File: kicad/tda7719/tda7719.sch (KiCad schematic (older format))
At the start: 15 parts

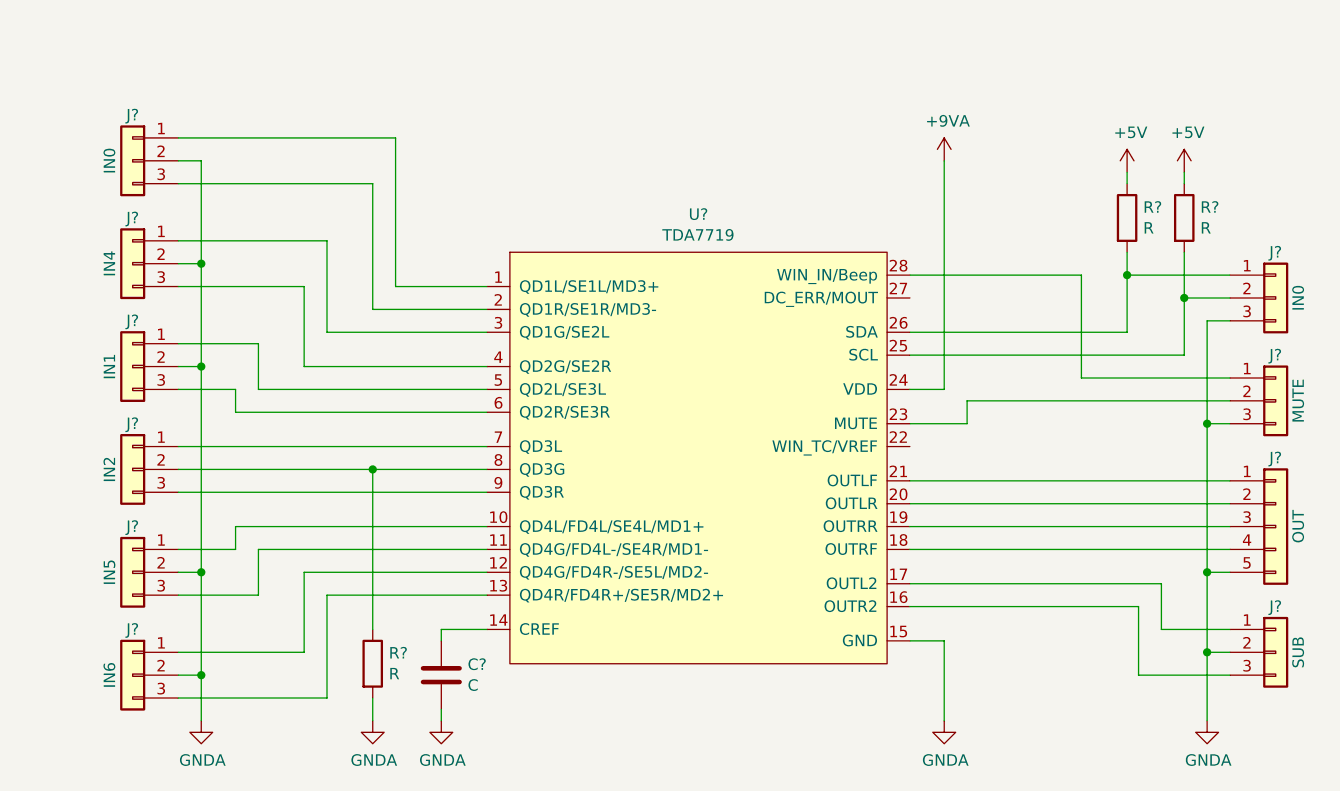
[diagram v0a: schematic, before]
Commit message: PCB for TDA7719
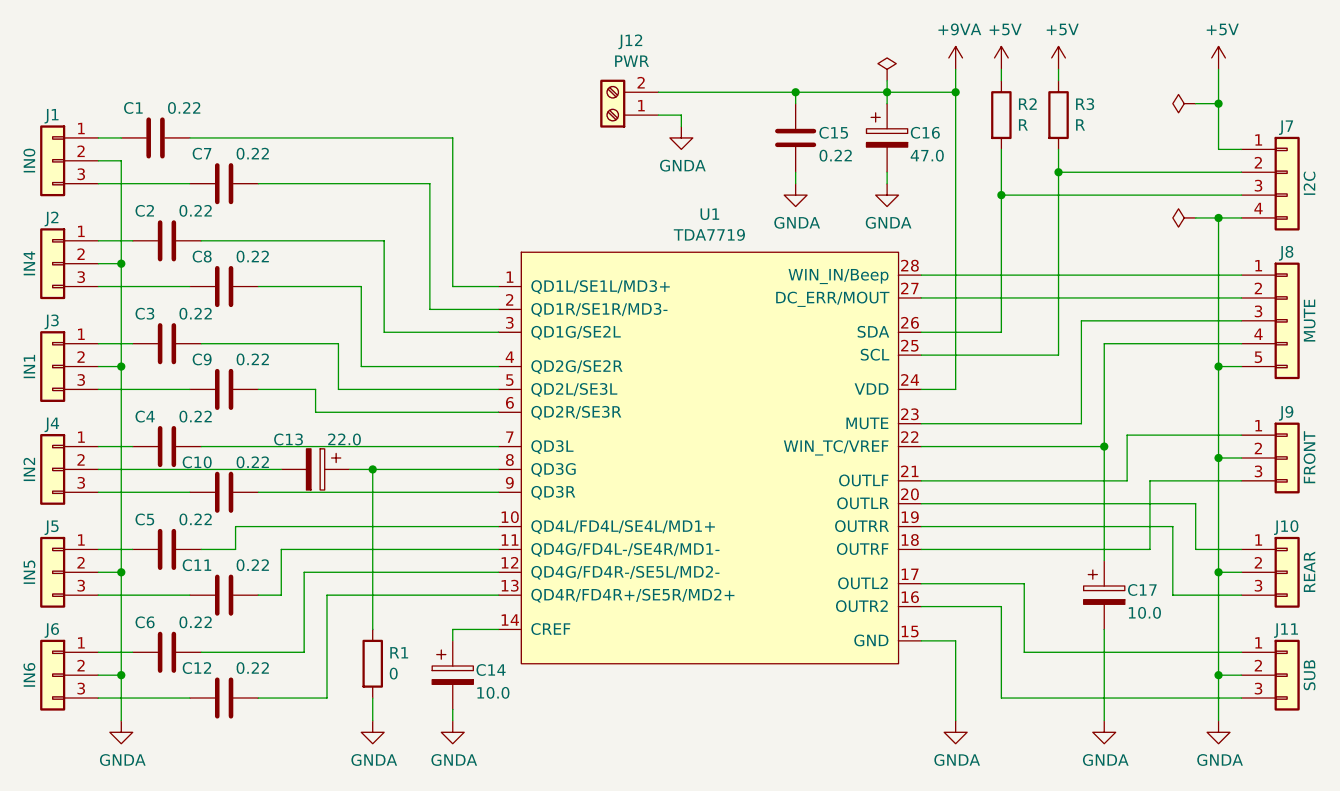
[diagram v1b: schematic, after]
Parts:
- removed C?: C, symbol Device:C
- removed J?: OUT, symbol Connector_Generic:Conn_01x05
- removed J?: IN0, symbol Connector_Generic:Conn_01x03
- removed J?: MUTE, symbol Connector_Generic:Conn_01x03
- added C1, C10, C11, C12, C15, C2, C3, C4, C5, C6, C7, C8, C9: 0.22, Capacitor_SMD:C_1206_3216Metric_Pad1.42x1.75mm_HandSolder, symbol Device:C
- added C13: 22.0, Capacitor_THT:CP_Radial_D5.0mm_P2.50mm, symbol Device:CP
- added C14, C17: 10.0, Capacitor_THT:CP_Radial_D5.0mm_P2.50mm, symbol Device:CP
- added C16: 47.0, Capacitor_THT:CP_Radial_D5.0mm_P2.50mm, symbol Device:CP
- added J10: REAR, Connector_PinHeader_2.54mm:PinHeader_1x03_P2.54mm_Vertical, symbol Connector_Generic:Conn_01x03
- added J12: PWR, TerminalBlock_Phoenix:TerminalBlock_Phoenix_MKDS-1,5-2-5.08_1x02_P5.08mm_Horizontal, symbol Connector:Screw_Terminal_01x02
- added J7: I2C, Connector_PinHeader_2.54mm:PinHeader_1x04_P2.54mm_Vertical, symbol Connector_Generic:Conn_01x04
- added J8: MUTE, Connector_PinHeader_2.54mm:PinHeader_1x05_P2.54mm_Vertical, symbol Connector_Generic:Conn_01x05
- added J9: FRONT, Connector_PinHeader_2.54mm:PinHeader_1x03_P2.54mm_Vertical, symbol Connector_Generic:Conn_01x03
- J1, J11, J2, J3, J4, J5, J6: renamed from J?; footprint (none) -> Connector_PinHeader_2.54mm:PinHeader_1x03_P2.54mm_Vertical
- R1: renamed from R?; value R -> 0; footprint (none) -> Resistor_SMD:R_1206_3216Metric_Pad1.42x1.75mm_HandSolder
- R2, R3: renamed from R?; footprint (none) -> Resistor_SMD:R_1206_3216Metric_Pad1.42x1.75mm_HandSolder
- gave numbers to parts that had none: 1
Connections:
- net +5V: now also J7.1 (Pin_1)
- net +9VA: now also C15.2, C16.1, J12.2 (Pin_2)
- net GNDA: now also C14.2, C15.1, C16.2, C17.2, J10.2 (Pin_2), J12.1 (Pin_1), J7.4 (Pin_4), J8.5 (Pin_5), J9.2 (Pin_2)
- net at U1.1 (QD1L/SE1L/MD3+): now also C1.1; no longer J1.1 (Pin_1)
- net at U1.10 (QD4L/FD4L/SE4L/MD1+): now also C5.1; no longer J5.1 (Pin_1)
- net at U1.11 (QD4G/FD4L-/SE4R/MD1-): now also C11.1; no longer J5.3 (Pin_3)
- net at U1.12 (QD4G/FD4R-/SE5L/MD2-): now also C6.1; no longer J6.1 (Pin_1)
- net at U1.13 (QD4R/FD4R+/SE5R/MD2+): now also C12.1; no longer J6.3 (Pin_3)
- net at U1.14 (CREF): now also C14.1
- net at U1.18 (OUTRF): now also J9.3 (Pin_3)
- net at U1.19 (OUTRR): now also J10.3 (Pin_3)
- net at U1.2 (QD1R/SE1R/MD3-): now also C7.1; no longer J1.3 (Pin_3)
- net at U1.20 (OUTLR): now also J10.1 (Pin_1)
- net at U1.21 (OUTLF): now also J9.1 (Pin_1)
- net at U1.22 (WIN_TC/VREF): now also C17.1, J8.4 (Pin_4)
- net at U1.23 (MUTE): now also J8.3 (Pin_3)
- net at R3.2, U1.25 (SCL): now also J7.2 (Pin_2)
- net at R2.2, U1.26 (SDA): now also J7.3 (Pin_3)
- net at U1.27 (DC_ERR/MOUT): now also J8.2 (Pin_2)
- net at U1.28 (WIN_IN/Beep): now also J8.1 (Pin_1)
- net at U1.3 (QD1G/SE2L): now also C2.1; no longer J2.1 (Pin_1)
- net at U1.4 (QD2G/SE2R): now also C8.1; no longer J2.3 (Pin_3)
- net at U1.5 (QD2L/SE3L): now also C3.1; no longer J3.1 (Pin_1)
- net at U1.6 (QD2R/SE3R): now also C9.1; no longer J3.3 (Pin_3)
- net at U1.7 (QD3L): now also C4.1; no longer J4.1 (Pin_1)
- net at R1.1, U1.8 (QD3G): now also C13.1; no longer J4.2 (Pin_2)
- net at U1.9 (QD3R): now also C10.1; no longer J4.3 (Pin_3)
- new net: C1.2, J1.1 (Pin_1)
- new net: C7.2, J1.3 (Pin_3)
- new net: C2.2, J2.1 (Pin_1)
- new net: C8.2, J2.3 (Pin_3)
- new net: C3.2, J3.1 (Pin_1)
- new net: C9.2, J3.3 (Pin_3)
- new net: C4.2, J4.1 (Pin_1)
- new net: C13.2, J4.2 (Pin_2)
- new net: C10.2, J4.3 (Pin_3)
- new net: C5.2, J5.1 (Pin_1)
- new net: C11.2, J5.3 (Pin_3)
- new net: C6.2, J6.1 (Pin_1)
- new net: C12.2, J6.3 (Pin_3)
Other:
- moved on the sheet: J1, J11, J2, J3, J4, J5, J6, R2, R3, U1
